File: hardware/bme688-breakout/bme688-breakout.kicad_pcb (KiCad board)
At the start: 2 copper layers, 38.1 x 27.9 mm, 35 parts, among them J1 Conn_01x08, J2 Conn_01x04, J3 Qwiic, J4 Qwiic, Q1 BSS138, Q2 BSS138, Q3 BSS138, Q4 BSS138, U1 BME688, U2 AP2112K-3.3

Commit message: Separate VIO from VIN so a 5V-powered board cannot overdrive a 3.3V host
Design review of the level shifters turned up a way to damage the host MCU.
The host-side pull-ups R3/R4/R6/R7 referenced VIN, so the four signal lines
idled at whatever the board was powered from. Run the board off 5V while
talking to a 3.3V part - ESP32, RP2040, STM32, the common case - and SCK,
SDI, SDO and CS all sit at 5V on 3.3V GPIO.

The pull-ups now reference a separate VIO rail, brought out on J1 pin 9
(the host header grows from 8 to 9 pins). JP4 bridges VIO to VIN as
manufactured, so the single-rail cases behave exactly as before and need
nothing done; a mixed-rail host cuts JP4 and feeds VIO from its own I/O
supply.

Also corrects the host logic range, which was claimed as 1.8-5.5V and was
never achievable. A BSS138 shifter needs its gate on the lower of the two
rails and the gate here is on the 3.3V sensor rail, so below 3.3V the FET
body diode (anode at the source, i.e. the sensor side) forward-biases and
pushes about VIO+0.7V back into the host. The real range is 3.3-5.5V;
1.8V logic would need a dual-supply translator, not a different resistor.
The board, silkscreen (front and back) and README all say so now.

VIO is drawn as a rail in the schematic, with its own power symbol in the
project library and a PWR_FLAG, matching how VIN and +3V3 are handled.

Board grows to 36 footprints and 15 nets; JP4 and the wider header are
placed clear of everything, the title moved out from under JP4, and the
whole design re-routed. All checks still pass: net assignment,
connectivity of all 15 nets, the simulated pour (85.8% copper, all 19 GND
items in one region), clearance, courtyards, outline, and the schematic
netlist matching design.py pin for pin.

Co-Authored-By: Claude Opus 5 <noreply@anthropic.com>
Claude-Session: https://claude.ai/code/session_012dyhR133MqMFAMEnBU7Qy6
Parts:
- added JP4: VIO_VIN, Jumper:SolderJumper-2_P1.3mm_Bridged_RoundedPad1.0x1.5mm, F.Cu at (104.5, 95.0)
- J1: value Conn_01x08 -> Conn_01x09; footprint Connector_PinHeader_2.54mm:PinHeader_1x08_P2.54mm_Vertical -> Connector_PinHeader_2.54mm:PinHeader_1x09_P2.54mm_Vertical
- moved J1 1.27 mm to (108.9, 100.4)
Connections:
- R3 pad 2: VIN -> VIO
- R4 pad 2: VIN -> VIO
- R6 pad 2: VIN -> VIO
- R7 pad 2: VIN -> VIO
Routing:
- net VIO: track 0.00 -> 23.3 mm, vias 0 -> 2
- net VIN: track 22.0 -> 28.3 mm, vias 2 -> 1
- net SCK_H: track 13.3 -> 16.3 mm, vias 1 -> 2
- net SDO_H: track 11.4 -> 10.0 mm
- net SDI_H: track 12.2 -> 11.0 mm
- net CS_H: track 10.2 -> 9.61 mm
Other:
- board text added: "VIN 2.5-5.5V -> on-board 3V3 LDO. Host logic = VIO, 3.3-5.5V."
- board text added: "VIO"
- board text added: "VIO = host I/O rail (3.3-5.5V). JP4 bridges it to VIN;"
- board text added: "VIO=VIN"
- board text added: "cut JP4 and feed VIO when host logic differs from VIN."
- board text removed: "BREAKOUT"
- board text removed: "VIN 2.5-5.5V -> on-board 3V3 LDO. Header logic 1.8-5.5V."

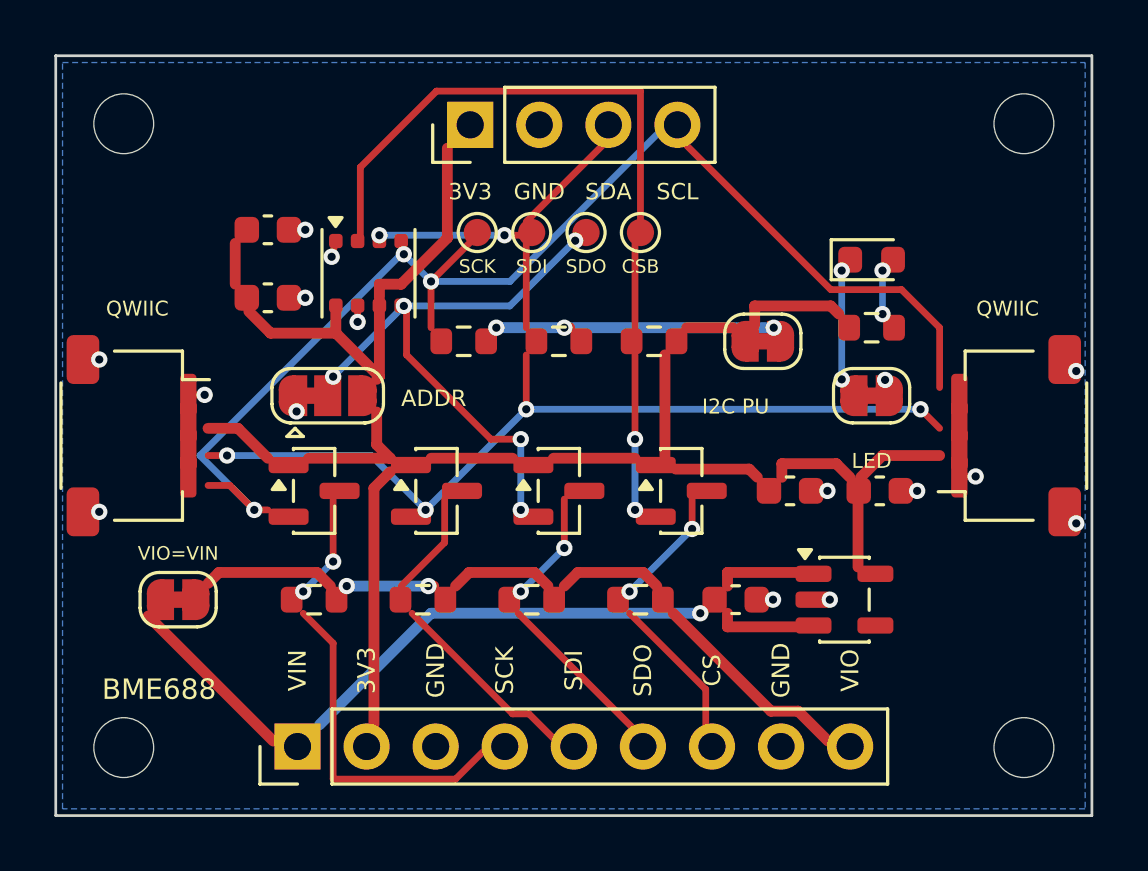
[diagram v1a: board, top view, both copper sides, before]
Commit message: Add the missing manufacturability checks, then fix the four bugs they found
The project file declared fabrication rules that nothing tested. Writing the
checks (scripts/dfm.py) turned up four real defects:

1. Copper too close to the board edge. verify.check_outline only asked
   whether copper was inside the outline, which a pad overhanging by 0.1mm
   satisfies. The Qwiic mounting pads sat 0.100mm from the routed edge
   against a 0.30mm min_copper_edge_clearance rule - introduced when the
   connectors were nudged inboard just far enough to get the pads on the
   board. Both connectors moved further in; C2 and C4 nudged to keep their
   courtyards clear. Edge gap is now exactly 0.300mm.

2. Ground stitching vias placed off-grid. gnd_vias tested the rounded grid
   cell for clearance but placed the via at the unrounded polar coordinate,
   so a via could drift up to half a cell past the clearance the grid had
   cleared - two landed 0.276mm from the edge. It now snaps to the cell it
   actually tested.

3. The ground pour fragmented. With the corrected geometry the pour split
   into two islands, stranding the ground pads that only reached the plane
   through a via in the orphan piece - caught by the pour-fill simulation,
   which is why it exists. B.Cu carries the pour, so every track put there
   cuts it; the via cost went 320 -> 1000 and routing is now ~82% front
   layer with the pour whole again.

4. A signal track ran under an M2 screw head. A metal screw on a grounded
   standoff would have shorted SCK_H to the pour below. Mounting holes are
   now a 3.8mm router keepout rather than a 2.2mm drill.

New checks: edge standoff, hole-to-hole web, annular ring, drill size, track
width, silkscreen text size, silk over copper, and copper under a screw head.
Silk over a via is reported as a note, not a warning, because the board tents
vias so they sit under solder mask.

Also documented, not changed: decoupling sits 3.3mm and 4.1mm from the pins
it serves, which t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
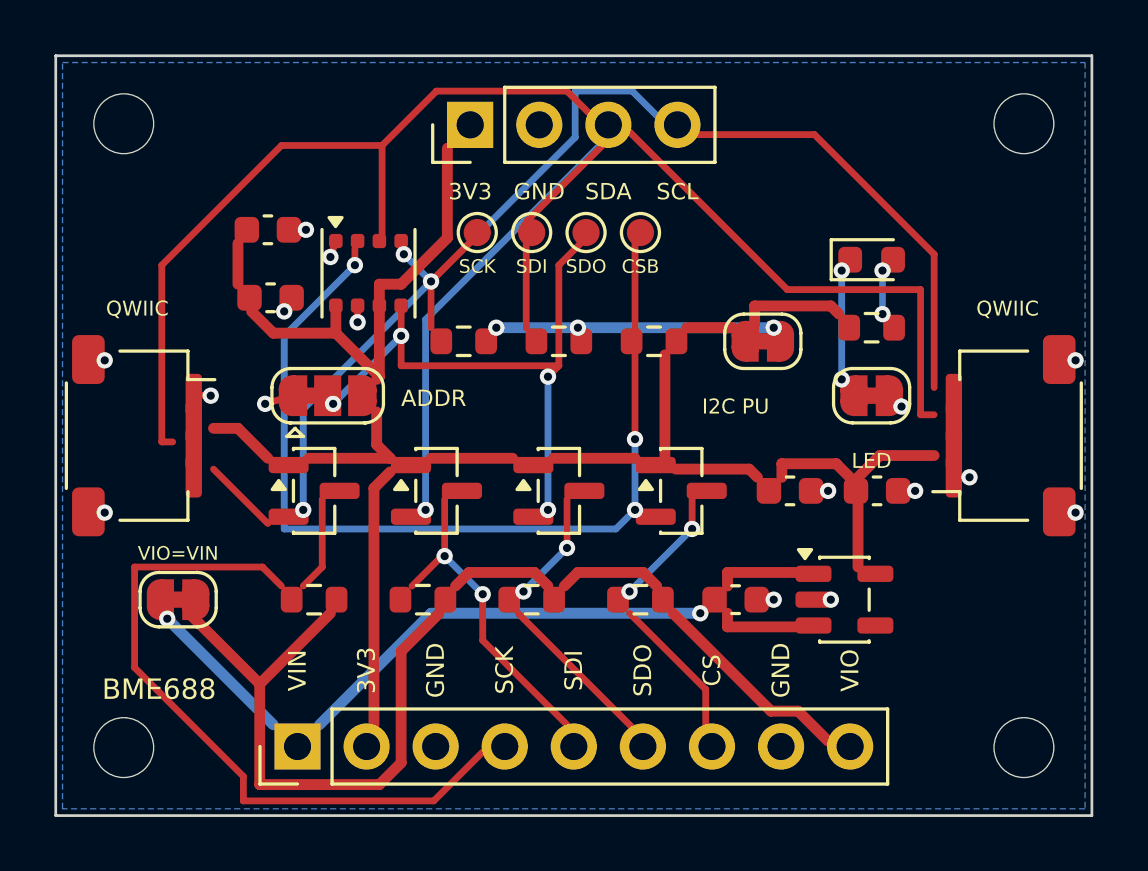
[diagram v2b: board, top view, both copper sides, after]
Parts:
- moved J3 0.20 mm to (103.1, 89.0)
- moved J4 0.20 mm to (135.0, 89.0)
- moved C4 0.10 mm to (130.2, 91.0)
- moved C2 0.10 mm to (107.9, 83.9)
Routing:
- net SDI: track 43.8 -> 70.2 mm, vias 6 -> 1
- net VIO: track 23.3 -> 37.8 mm, vias 2 -> 0
- net SCK_H: track 16.3 -> 29.0 mm, vias 2 -> 0
- net CSB: track 27.6 -> 33.4 mm, vias 2 -> 3
- net SDI_H: track 11.0 -> 11.9 mm, vias 0 -> 2
- net VIN: track 28.3 -> 27.4 mm, vias 1 -> 2
- net SDO: track 20.8 -> 21.6 mm, vias 5 -> 4
- net GND: track 9.60 -> 10.2 mm
